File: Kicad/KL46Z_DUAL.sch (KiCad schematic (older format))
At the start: 2 parts, among them J15 __FREEDOM_X, J16 __FREEDOM_X

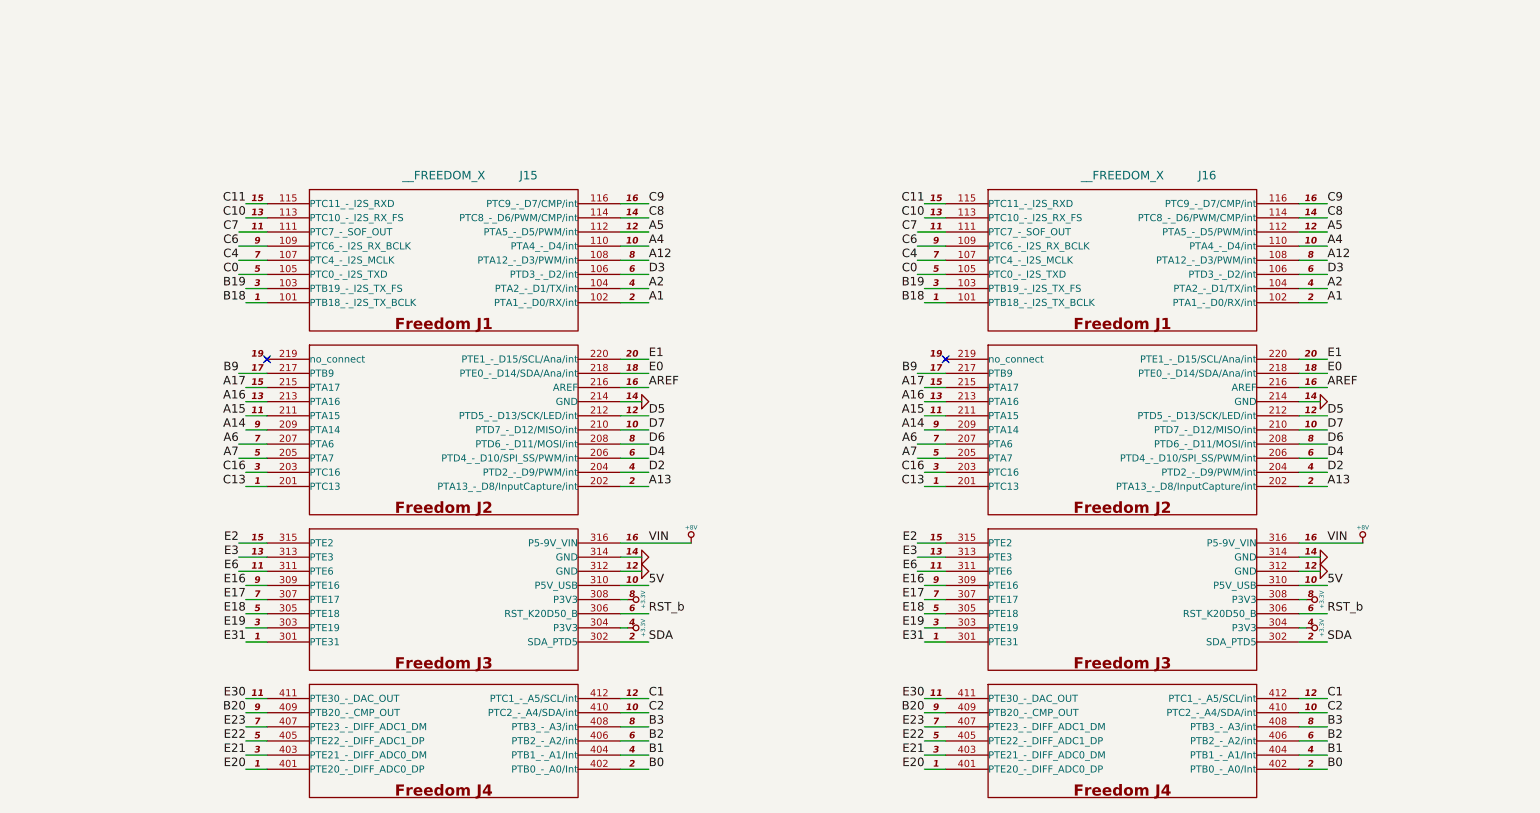
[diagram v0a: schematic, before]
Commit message: 
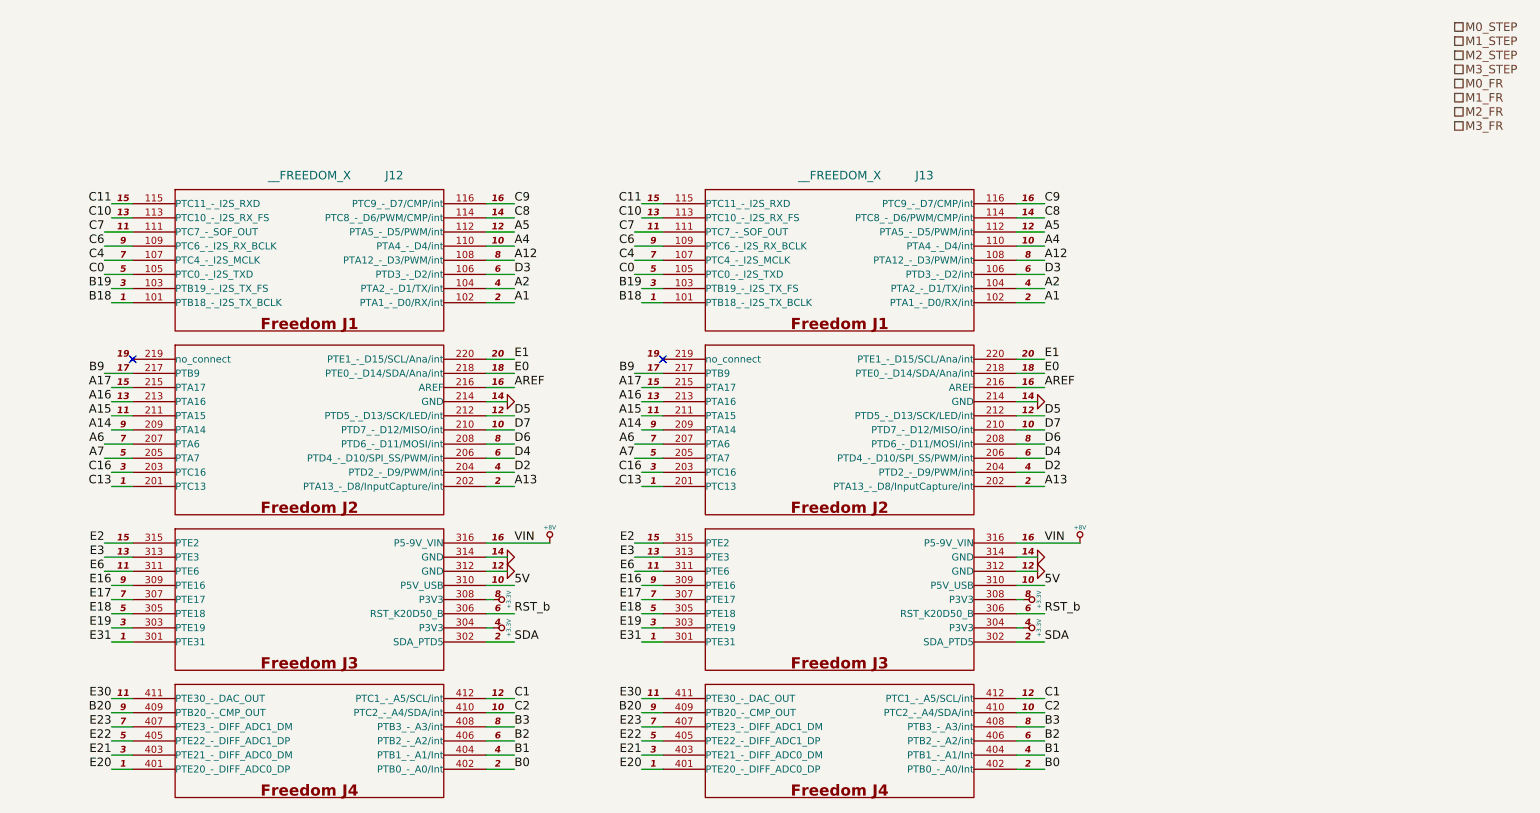
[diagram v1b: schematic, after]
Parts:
- renumbered J15 to J12, J16 to J13
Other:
- moved on the sheet: J12, J13

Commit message: All wired. ERC passes with no errors. Might be good to go.
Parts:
- renumbered J12 to J10, J13 to J11
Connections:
- net D2 is gone; now on net M0_STEP: J10.204 (PTD2_-_D9/PWM/int), J11.204 (PTD2_-_D9/PWM/int)
- net D3 is gone; now on net M1_STEP: J10.106 (PTD3_-_D2/int), J11.106 (PTD3_-_D2/int)
- net D4 is gone; now on net M2_STEP: J10.206 (PTD4_-_D10/SPI_SS/PWM/int), J11.206 (PTD4_-_D10/SPI_SS/PWM/int)
- net D5 is gone; now on net M3_STEP: J10.212 (PTD5_-_D13/SCK/LED/int), J11.212 (PTD5_-_D13/SCK/LED/int)
- net E0 is gone; now on net M0_FR: J10.218 (PTE0_-_D14/SDA/Ana/int), J11.218 (PTE0_-_D14/SDA/Ana/int)
- net E1 is gone; now on net M1_FR: J10.220 (PTE1_-_D15/SCL/Ana/int), J11.220 (PTE1_-_D15/SCL/Ana/int)
- net E2 is gone; now on net M2_FR: J10.315 (PTE2), J11.315 (PTE2)
- net E3 is gone; now on net M3_FR: J10.313 (PTE3), J11.313 (PTE3)
- net D6 renamed X_RX
- net D7 renamed X_TX
- net E16 renamed M_CS
- net E17 renamed SCL
- net E18 renamed SDATA
- net E19 renamed L_CS
- net E20 renamed X_ON
- net E21 renamed X_RESET_b
- net E30 renamed M_VREF
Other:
- moved on the sheet: J10

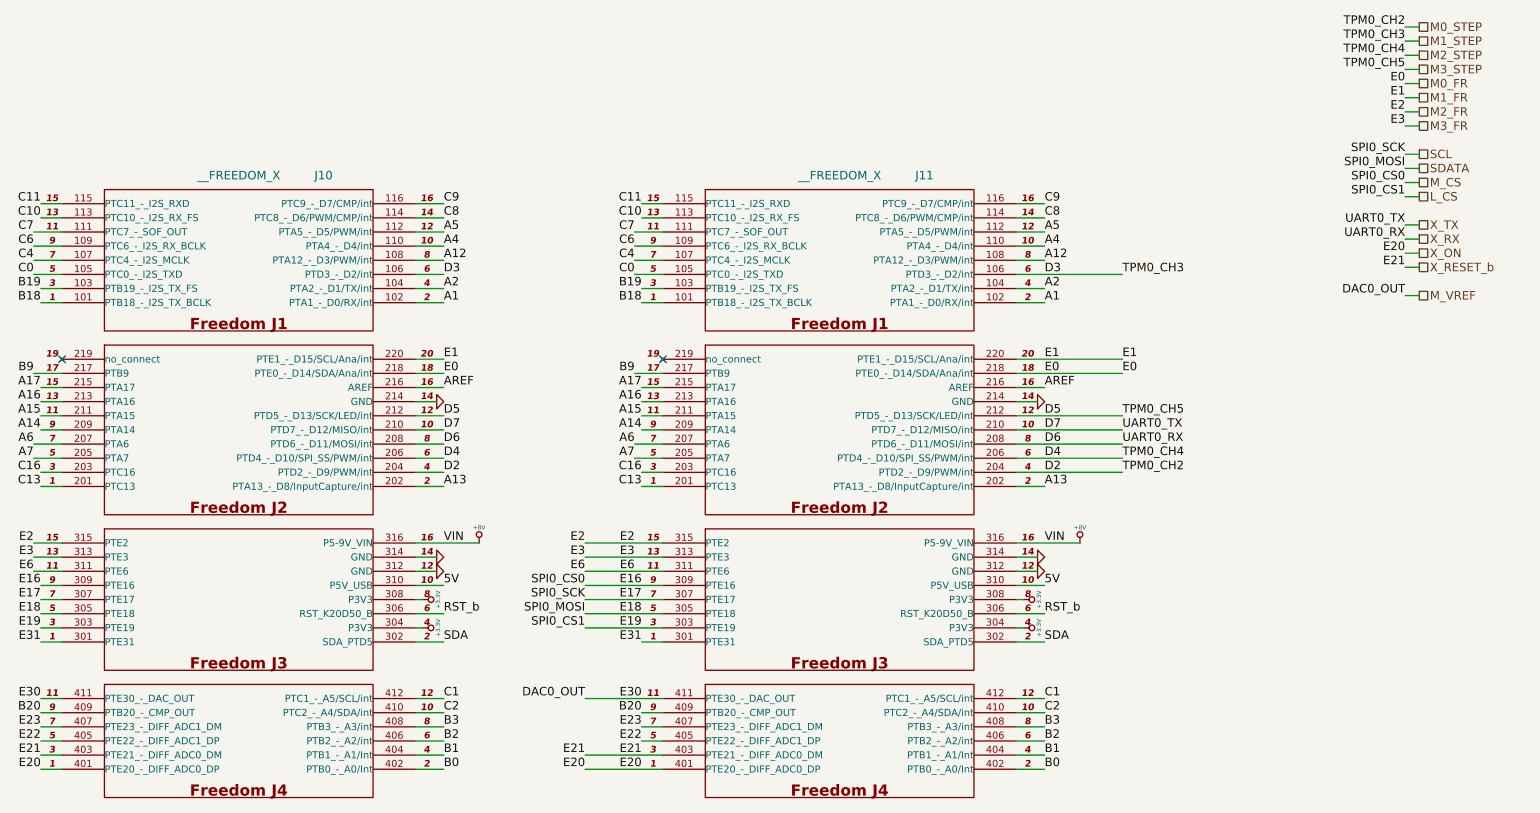
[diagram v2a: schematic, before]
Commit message: 
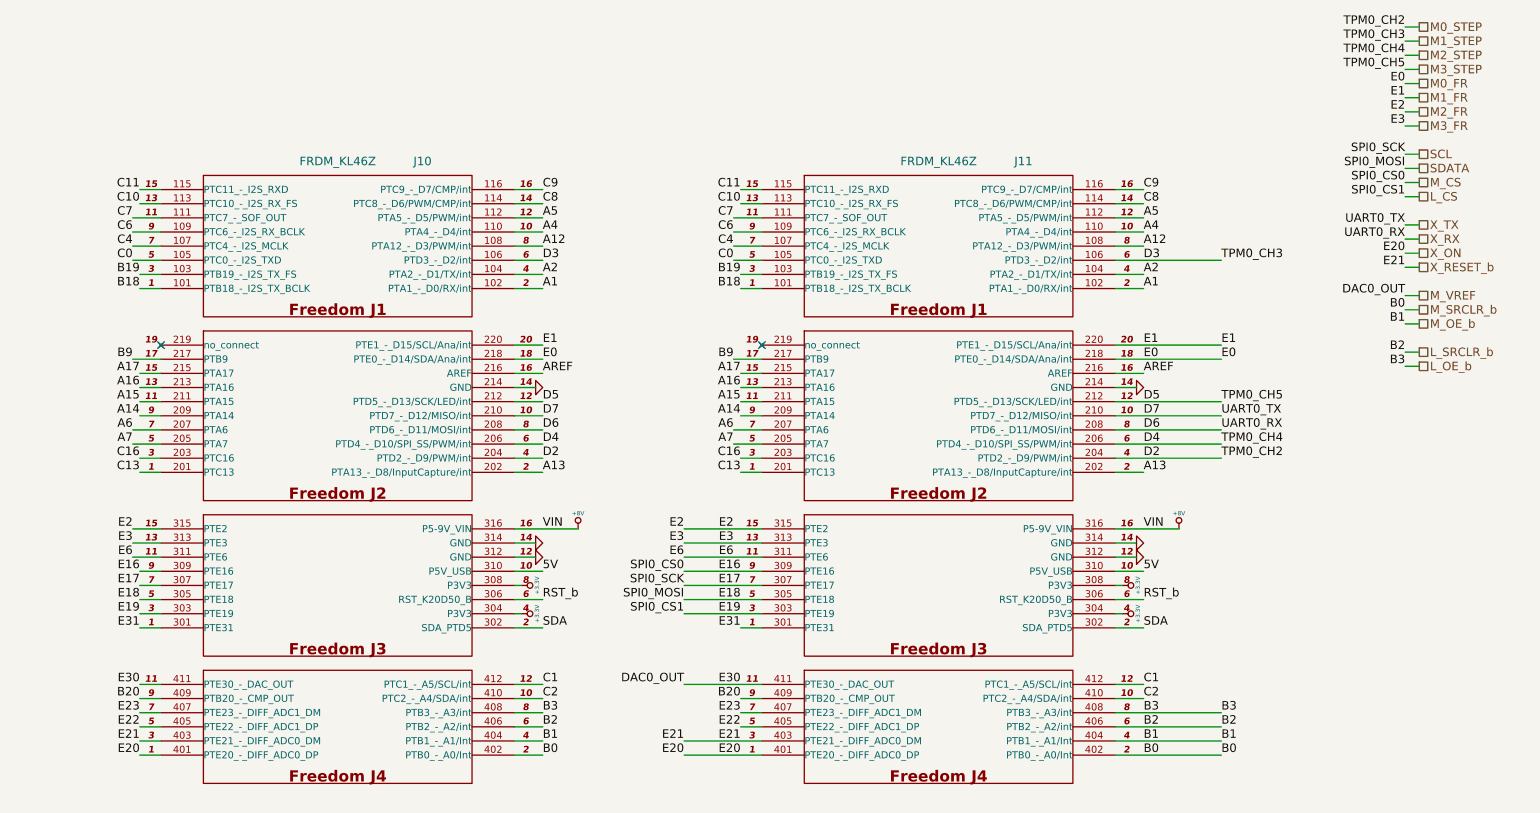
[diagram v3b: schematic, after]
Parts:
- J10, J11: value __FREEDOM_X -> FRDM_KL46Z
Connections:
- net B0 renamed M_SRCLR_b
- net B1 renamed M_OE_b
- net B2 renamed L_SRCLR_b
- net B3 renamed L_OE_b
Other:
- moved on the sheet: J10, J11

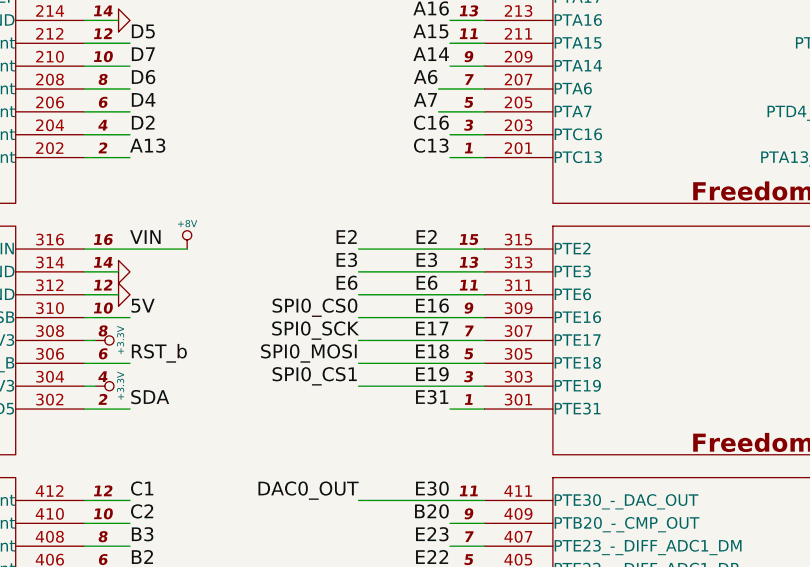
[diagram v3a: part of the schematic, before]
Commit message: 
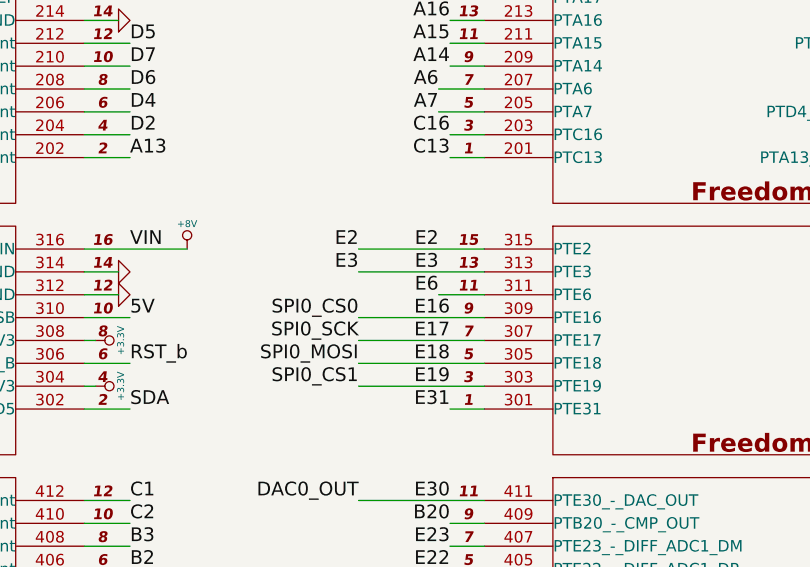
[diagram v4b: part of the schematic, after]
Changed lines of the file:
@@
 LIBS:contrib
 LIBS:valves
-LIBS:___power_diode
-LIBS:__batterybarlug
-LIBS:__freedom_x
-LIBS:__xbee-pro
-LIBS:CAR
 LIBS:car_v3-cache
 EELAYER 27 0
@@
 Sheet 11 15
 Title ""
-Date "8 jun 2014"
+Date "13 jul 2014"
 Rev ""
 Comp ""
@@
 Text HLabel 10450 2400 2    60   UnSpc ~ 0
 X_RESET_b
-Text Label 5250 4450 2    60   ~ 0
-E6
 Text Label 5250 5350 2    60   ~ 0
 DAC0_OUT
@@
 	5250 4550 5800 4550
 Wire Wire Line
-	5250 4450 5800 4450
-Wire Wire Line
 	5250 4350 5800 4350
 Wire Wire Line
@@
 Wire Wire Line
 	10350 3100 10450 3100
+Wire Wire Line
+	5800 4450 5600 4450
 $EndSCHEMATC

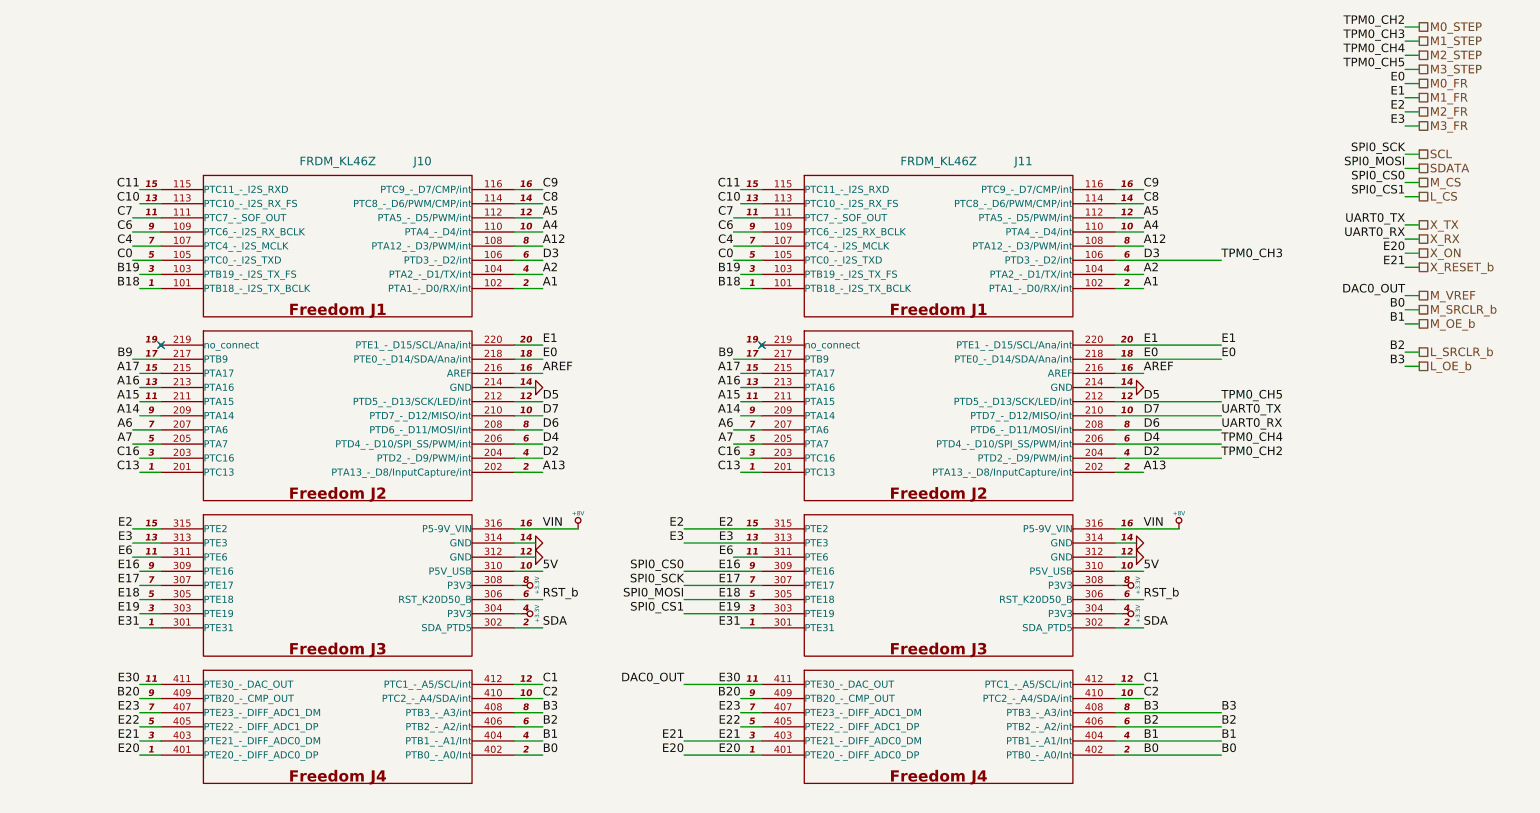
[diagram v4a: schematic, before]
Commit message: 
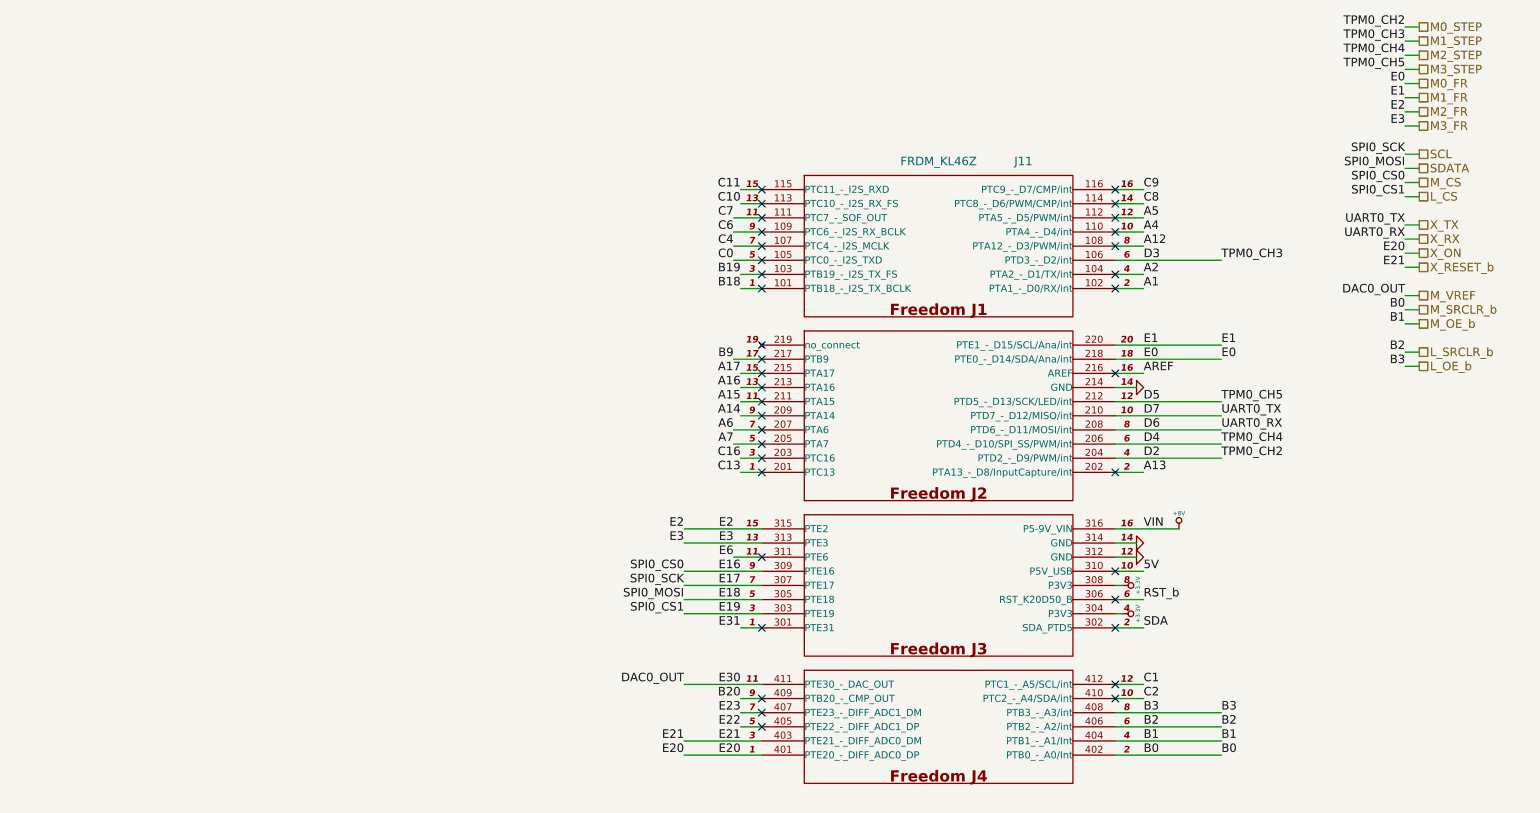
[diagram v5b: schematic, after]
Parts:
- removed J10: FRDM_KL46Z, ~, symbol __FREEDOM_X
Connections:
- no-connect marks 2 -> 37
